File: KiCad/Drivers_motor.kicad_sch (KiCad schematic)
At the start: 5 parts, among them M1 Motor_DC, SW1 SW_SPST, U1 L298N

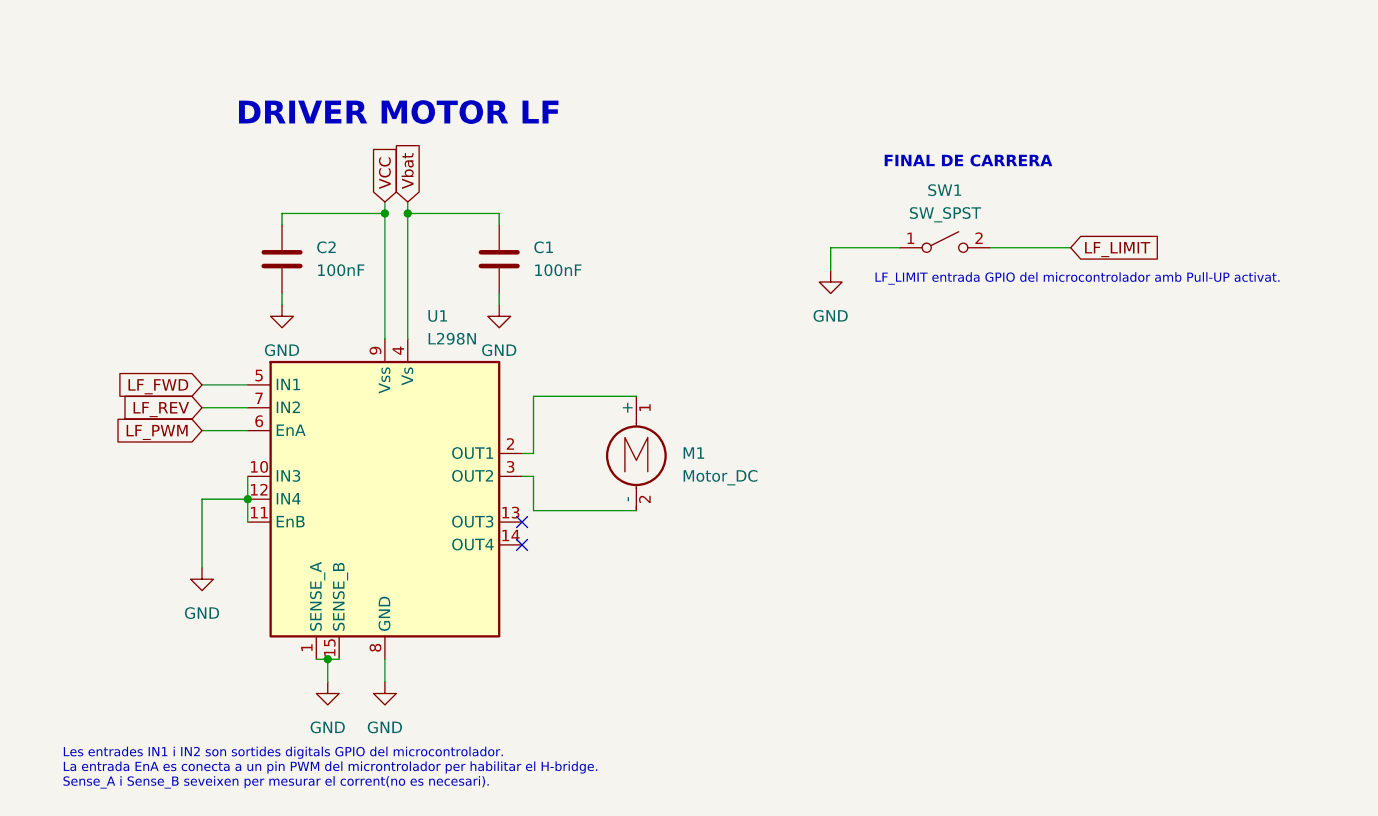
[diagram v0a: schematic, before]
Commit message: acabar can, estil y micro biel
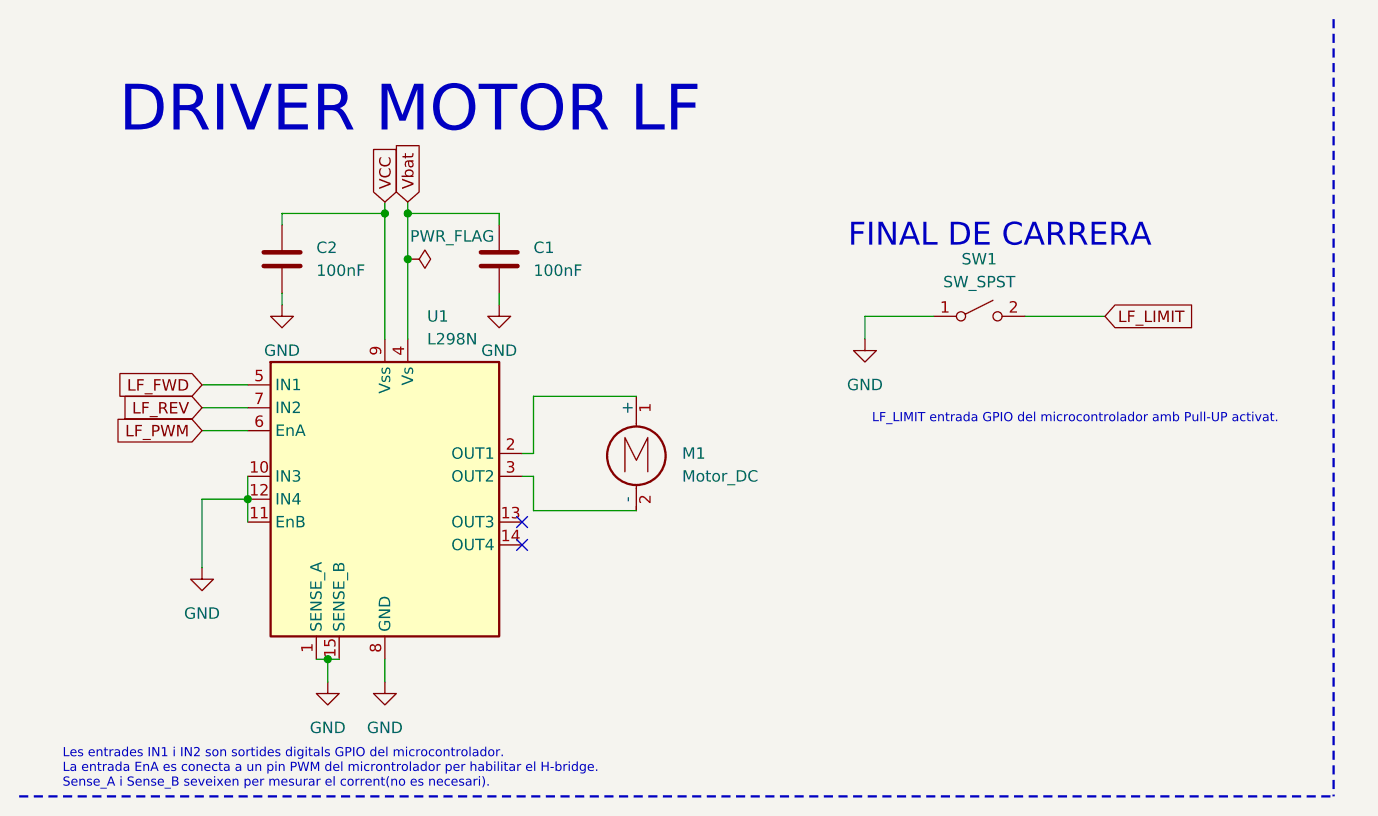
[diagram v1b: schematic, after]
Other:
- moved on the sheet: SW1
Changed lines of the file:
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@@
 	(text "LF_LIMIT entrada GPIO del microcontrolador amb Pull-UP activat."
 		(exclude_from_sim no)
-		(at 130.302 41.656 0)
+		(at 130.048 57.15 0)
 		(effects
 			(font
 				(size 1.016 1.016)
-			)
-		)
-	)
-	(text "FINAL DE CARRERA"
-		(exclude_from_sim no)
-		(at 118.11 28.702 0)
+				(color 0 0 0 1)
+			)
+		)
+	)
+	(text "DRIVER MOTOR LF"
+		(exclude_from_sim no)
+		(at 56.134 22.86 0)
 		(effects
 			(font
-				(size 1.27 1.27)
-				(thickness 0.254)
-				(bold yes)
-			)
-		)
-	)
-	(text "DRIVER MOTOR LF"
-		(exclude_from_sim no)
-		(at 54.864 23.368 0)
+				(size 5.08 5.08)
+				(color 0 0 0 1)
+			)
+		)
+	)
+	(text "FINAL DE CARRERA"
+		(exclude_from_sim no)
+		(at 121.666 36.83 0)
 		(effects
 			(font
 				(size 2.54 2.54)
-				(thickness 0.254)
-				(bold yes)
+				(color 0 0 0 1)
 			)
 		)
@@
 			(font
 				(size 1.016 1.016)
+				(color 0 0 0 1)
 			)
 			(justify left)
@@
 	)
 	(junction
+		(at 55.88 39.37)
+		(diameter 0)
+		(color 0 0 0 0)
+	)
+	(junction
 		(at 53.34 34.29)
 		(diameter 0)
@@
 	(wire
 		(pts
-			(xy 102.87 38.1) (xy 102.87 40.64)
+			(xy 106.68 45.72) (xy 106.68 48.26)
 		)
 		(stroke
@@
 	(wire
 		(pts
+			(xy 55.88 39.37) (xy 55.88 48.26)
+		)
+		(stroke
+			(width 0)
+			(type default)
+		)
+	)
+	(wire
+		(pts
 			(xy 46.99 83.82) (xy 48.26 83.82)
 		)
@@
 		)
 	)
+	(polyline
+		(pts
+			(xy 158.75 12.7) (xy 158.75 99.06)
+		)
+		(stroke
+			(width 0.254)
+			(type dash)
+			(color 0 0 0 1)
+		)
+	)
 	(wire
 		(pts
@@
 	(wire
 		(pts
-			(xy 55.88 34.29) (xy 55.88 48.26)
-		)
-		(stroke
-			(width 0)
-			(type default)
-		)
-	)
-	(wire
-		(pts
-			(xy 110.49 38.1) (xy 102.87 38.1)
-		)
-		(stroke
-			(width 0)
-			(type default)
+			(xy 55.88 34.29) (xy 55.88 39.37)
+		)
+		(stroke
+			(width 0)
+			(type default)
+		)
+	)
+	(wire
+		(pts
+			(xy 114.3 45.72) (xy 106.68 45.72)
+		)
+		(stroke
+			(width 0)
+			(type default)
+		)
+	)
+	(polyline
+		(pts
+			(xy 12.7 99.06) (xy 158.75 99.06)
+		)
+		(stroke
+			(width 0.254)
+			(type dash)
+			(color 0 0 0 1)
 		)
 	)
@@
 	(wire
 		(pts
-			(xy 120.65 38.1) (xy 129.54 38.1)
+			(xy 124.46 45.72) (xy 133.35 45.72)
 		)
 		(stroke
@@
 	(global_label "LF_LIMIT"
 		(shape input)
-		(at 129.54 38.1 0)
+		(at 133.35 45.72 0)
 		(fields_autoplaced yes)
 		(effects
@@
 		)
 		(property "Intersheetrefs" "${INTERSHEET_REFS}"
-			(at 140.2662 38.1 0)
+			(at 144.0762 45.72 0)
 			(effects
 				(font
@@
 	(symbol
 		(lib_id "Switch:SW_SPST")
-		(at 115.57 38.1 0)
+		(at 119.38 45.72 0)
 		(unit 1)
 		(exclude_from_sim no)
@@
 		(fields_autoplaced yes)
 		(property "Reference" "SW1"
-			(at 115.57 31.75 0)
+			(at 119.38 39.37 0)
 			(effects
 				(font
@@
 		)
 		(property "Value" "SW_SPST"
-			(at 115.57 34.29 0)
+			(at 119.38 41.91 0)
 			(effects
 				(font
@@
 		)
 		(property "Footprint" ""
-			(at 115.57 38.1 0)
+			(at 119.38 45.72 0)
 			(effects
 				(font
@@
 		)
 		(property "Datasheet" "~"
-			(at 115.57 38.1 0)
+			(at 119.38 45.72 0)
 			(effects
 				(font
@@
 		)
 		(property "Description" "Single Pole Single Throw (SPST) switch"
-			(at 115.57 38.1 0)
+			(at 119.38 45.72 0)
 			(effects
 				(font
@@
 	)
 	(symbol
+		(lib_id "power:PWR_FLAG")
+		(at 55.88 39.37 270)
+		(unit 1)
+		(exclude_from_sim no)
+		(in_bom yes)
+		(on_board yes)
+		(dnp no)
+		(property "Reference" "#FLG02"
+			(at 57.785 39.37 0)
+			(effects
+				(font
+					(size 1.27 1.27)
+				)
+				(hide yes)
+			)
+		)
+		(property "Value" "PWR_FLAG"
+			(at 56.134 36.83 90)
+			(effects
+				(font
+					(size 1.27 1.27)
+				)
+				(justify left)
+			)
+		)
+		(property "Footprint" ""
+			(at 55.88 39.37 0)
+			(effects
+				(font
+					(size 1.27 1.27)
+				)
+				(hide yes)
+			)
+		)
+		(property "Datasheet" "~"
+			(at 55.88 39.37 0)
+			(effects
+				(font
+					(size 1.27 1.27)
+				)
+				(hide yes)
+			)
+		)
+		(property "Description" "Special symbol for telling ERC where power comes from"
+			(at 55.88 39.37 0)
+			(effects
+				(font
+					(size 1.27 1.27)
+				)
+				(hide yes)
+			)
+		)
+		(pin "1"
+		)
+		(instances
+			(project ""
+				(path "/88ef36bc-9439-47f2-adb5-e1da6bb8c9dd/084d3e4b-4417-484c-9f12-9be60a63d6ad"
+					(reference "#FLG02")
+					(unit 1)
+				)
+			)
+		)
+	)
+	(symbol
 		(lib_id "power:GND")
 		(at 66.04 44.45 0)
@@
 	(symbol
 		(lib_id "power:GND")
-		(at 102.87 40.64 0)
+		(at 106.68 48.26 0)
 		(unit 1)
 		(exclude_from_sim no)
@@
 		(fields_autoplaced yes)
 		(property "Reference" "#PWR06"
-			(at 102.87 46.99 0)
+			(at 106.68 54.61 0)
 			(effects
 				(font
@@
 		)
 		(property "Value" "GND"
-			(at 102.87 45.72 0)
+			(at 106.68 53.34 0)
 			(effects
 				(font
@@
 		)
 		(property "Footprint" ""
-			(at 102.87 40.64 0)
+			(at 106.68 48.26 0)
 			(effects
 				(font
@@
 		)
 		(property "Datasheet" ""
-			(at 102.87 40.64 0)
+			(at 106.68 48.26 0)
 			(effects
 				(font
@@
 		)
 		(property "Description" "Power symbol creates a global label with name \"GND\" , ground"
-			(at 102.87 40.64 0)
-			(effects
-				(font
+			(at 106.68 48.26 0)
+			(effects
+				(font

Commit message: Debugging
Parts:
- removed C1: 100nF, symbol Device:C
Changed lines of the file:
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@@
-	)
-	(junction
-		(at 55.88 34.29)
-		(diameter 0)
-		(color 0 0 0 0)
 	)
 	(junction
@@
 	(wire
 		(pts
-			(xy 66.04 43.18) (xy 66.04 44.45)
-		)
-		(stroke
-			(width 0)
-			(type default)
-		)
-	)
-	(wire
-		(pts
 			(xy 53.34 33.02) (xy 53.34 34.29)
 		)
@@
 	(wire
 		(pts
-			(xy 55.88 34.29) (xy 55.88 33.02)
-		)
-		(stroke
-			(width 0)
-			(type default)
-		)
-	)
-	(wire
-		(pts
-			(xy 55.88 34.29) (xy 66.04 34.29)
-		)
-		(stroke
-			(width 0)
-			(type default)
-		)
-	)
-	(wire
-		(pts
 			(xy 33.02 66.04) (xy 33.02 73.66)
 		)
@@
 		(pts
 			(xy 69.85 67.31) (xy 81.28 67.31)
-		)
-		(stroke
-			(width 0)
-			(type default)
-		)
-	)
-	(wire
-		(pts
-			(xy 66.04 34.29) (xy 66.04 35.56)
 		)
 		(stroke
@@
 	(wire
 		(pts
-			(xy 55.88 34.29) (xy 55.88 39.37)
+			(xy 55.88 33.02) (xy 55.88 39.37)
 		)
 		(stroke
@@
 				(path "/88ef36bc-9439-47f2-adb5-e1da6bb8c9dd/084d3e4b-4417-484c-9f12-9be60a63d6ad"
 					(reference "#PWR05")
-					(unit 1)
-				)
-			)
-		)
-	)
-	(symbol
-		(lib_id "Device:C")
-		(at 66.04 39.37 0)
-		(unit 1)
-		(exclude_from_sim no)
-		(in_bom yes)
-		(on_board yes)
-		(dnp no)
-		(fields_autoplaced yes)
-		(property "Reference" "C1"
-			(at 69.85 38.0999 0)
-			(effects
-				(font
-					(size 1.27 1.27)
-				)
-				(justify left)
-			)
-		)
-		(property "Value" "100nF"
-			(at 69.85 40.6399 0)
-			(effects
-				(font
-					(size 1.27 1.27)
-				)
-				(justify left)
-			)
-		)
-		(property "Footprint" ""
-			(at 67.0052 43.18 0)
-			(effects
-				(font
-					(size 1.27 1.27)
-				)
-				(hide yes)
-			)
-		)
-		(property "Datasheet" "~"
-			(at 66.04 39.37 0)
-			(effects
-				(font
-					(size 1.27 1.27)
-				)
-				(hide yes)
-			)
-		)
-		(property "Description" "Unpolarized capacitor"
-			(at 66.04 39.37 0)
-			(effects
-				(font
-					(size 1.27 1.27)
-				)
-				(hide yes)
-			)
-		)
-		(pin "2"
-		)
-		(pin "1"
-		)
-		(instances
-			(project "Grup_D_Llums"
-				(path "/88ef36bc-9439-47f2-adb5-e1da6bb8c9dd/084d3e4b-4417-484c-9f12-9be60a63d6ad"
-					(reference "C1")
 					(unit 1)
 				)
@@
 					(unit 1)
 				)
-			)
-		)
-	)
-	(symbol
-		(lib_id "power:GND")
-		(at 66.04 44.45 0)
-		(unit 1)
-		(exclude_from_sim no)
-		(in_bom yes)
-		(on_board yes)
-		(dnp no)
-		(fields_autoplaced yes)
-		(property "Reference" "#PWR03"
-			(at 66.04 50.8 0)
-			(effects
-				(font
-					(size 1.27 1.27)
-				)
-				(hide yes)
-			)
-		)
-		(property "Value" "GND"
-			(at 66.04 49.53 0)
-			(effects
-				(font
-					(size 1.27 1.27)
-				)
-			)
-		)
-		(property "Footprint" ""
-			(at 66.04 44.45 0)
-			(effects
-				(font
-					(size 1.27 1.27)
-				)
-				(hide yes)
-			)
-		)
-		(property "Datasheet" ""
-			(at 66.04 44.45 0)
-			(effects
-				(font
-					(size 1.27 1.27)
-				)
-				(hide yes)
-			)
-		)
-		(property "Description" "Power symbol creates a global label with name \"GND\" , ground"
-			(at 66.04 44.45 0)
-			(effects
-				(font
-					(size 1.27 1.27)
-				)
-				(hide yes)
-			)
-		)
-		(pin "1"
-		)
-		(instances
-			(project "Grup_D_Llums"
-				(path "/88ef36bc-9439-47f2-adb5-e1da6bb8c9dd/084d3e4b-4417-484c-9f12-9be60a63d6ad"
-					(reference "#PWR03")
-					(unit 1)
-				)
